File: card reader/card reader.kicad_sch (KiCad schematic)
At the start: 0 parts

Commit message: pdf
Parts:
- added A1: Arduino_Nano_v3.x, Module:Arduino_Nano, symbol MCU_Module:Arduino_Nano_v3.x
- added Q7: 2N7000, Package_TO_SOT_THT:TO-92_Inline, symbol Transistor_FET:2N7000
- added R1, R2, R26, R27, R3: 10k, symbol Device:R
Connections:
- new net: R2.2, R3.1
- new net +3.3V: Q7.2 (G), R26.1
- new net +5V: R27.1
- new net GND: R3.2
- new net RX_ARDUINO: Q7.3 (D), R27.2
- new net RX_RFID: R1.2, R2.1
- new net TX_ARDUINO: R1.1
- new net TX_RFID: Q7.1 (S), R26.2
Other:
- note added: "Adaptamos la tensión de 5 V a ~3.3 V (Arduino -> RFID reader)"
- note added: "Definir si se usa SPI o serial por soft. Seguramente si es spi se necesitan 3/4 conversores, si es serial solo 1 activo 1 pasivo. si es I2C idem serial"
- note added: "Esto es SPI seguro, al parecer es hard-wired"
- note added: "Subimos la tensión de 3.3 V a 5 V (RFID reader -> Arduino)"
- note added: "https://circuitdigest.com/microcontroller-projects/interfacing-rfid-reader-module-with-arduino"

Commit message: lolin module
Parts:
- removed A1: Arduino_Nano_v3.x, Module:Arduino_Nano, symbol MCU_Module:Arduino_Nano_v3.x
- removed Q7: 2N7000, Package_TO_SOT_THT:TO-92_Inline, symbol Transistor_FET:2N7000
- removed R1, R2, R26, R27, R3: 10k, symbol Device:R
- added M1: RFID-RC522, RFID-RC522:RFID-RC522, symbol RFID-RC522:RFID-RC522
- added U1: NodeMCU1.0(ESP-12E), ESP8266:NodeMCU-LoLinV3, symbol ESP8266:NodeMCU1.0(ESP-12E)
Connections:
- net +3.3V: now also M1.8 (3V3), U1.16 (3.3V)
- net GND: now also M1.6 (GND), U1.17 (GND)
- new net miso: M1.4 (MISO), U1.22 (D6(GPIO12))
- new net mosi: M1.3 (MOSI), U1.21 (D7(GPIO13))
- new net rst: M1.7 (RST), U1.27 (D3(GPIO0))
- new net sck: M1.2 (SCK), U1.23 (D5(GPIO14))
- new net sda: M1.1 (SDA), U1.26 (D4(GPIO2))
- no-connect marks 0 -> 1
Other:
- note added: "RFID RC522 (SPI) -> NodeMCU v1 (ESP-12E) SDA (SS) -> D4 (GPIO2) SCK -> D5 (GPIO14) MOSI -> D7 (GPIO13) MISO -> D6 (GPIO12) RST -> D3 (GPIO0) 3V3 -> 3V3 GND -> GND"
- note removed: "Adaptamos la tensión de 5 V a ~3.3 V (Arduino -> RFID reader)"
- note removed: "Definir si se usa SPI o serial por soft. Seguramente si es spi se necesitan 3/4 conversores, si es serial solo 1 activo 1 pasivo. si es I2C idem serial"
- note removed: "Esto es SPI seguro, al parecer es hard-wired"
- note removed: "Subimos la tensión de 3.3 V a 5 V (RFID reader -> Arduino)"
- note removed: "https://circuitdigest.com/microcontroller-projects/interfacing-rfid-reader-module-with-arduino"

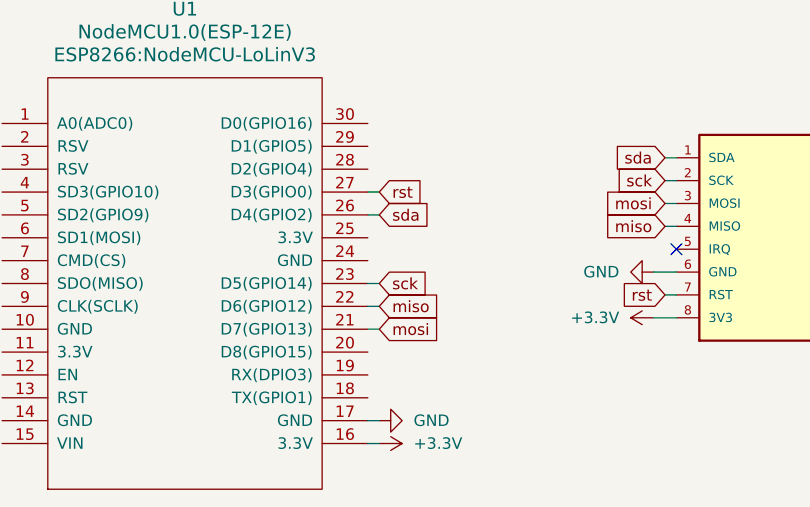
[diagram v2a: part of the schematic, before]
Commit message: ajustes,  1 nodemcu anda mal
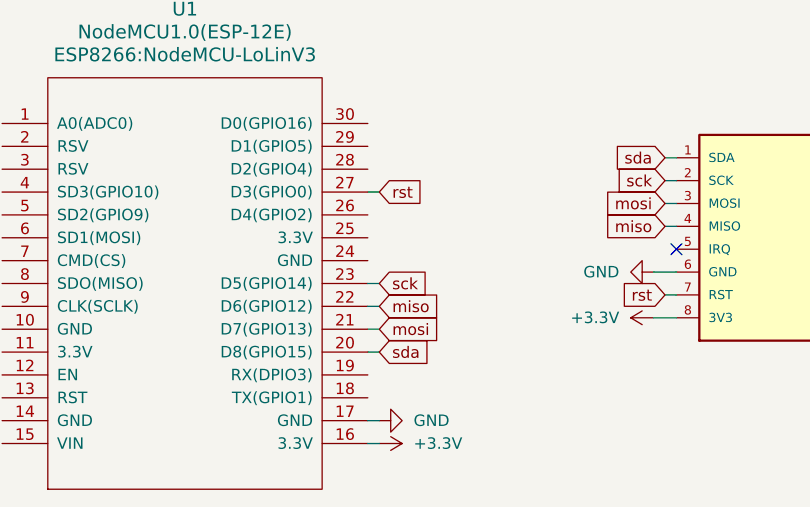
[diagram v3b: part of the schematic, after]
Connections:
- net sda: now also U1.20 (D8(GPIO15)); no longer U1.26 (D4(GPIO2))
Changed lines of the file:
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@@
 	(wire
 		(pts
-			(xy 125.73 102.87) (xy 124.46 102.87)
+			(xy 157.48 99.06) (xy 158.75 99.06)
 		)
 		(stroke
@@
 	(wire
 		(pts
-			(xy 157.48 99.06) (xy 158.75 99.06)
+			(xy 124.46 118.11) (xy 125.73 118.11)
 		)
 		(stroke
@@
 	(global_label "sda"
 		(shape input)
-		(at 125.73 102.87 0)
+		(at 125.73 118.11 0)
 		(fields_autoplaced yes)
 		(effects
@@
 		)
 		(property "Intersheetrefs" "${INTERSHEET_REFS}"
-			(at 132.0413 102.87 0)
+			(at 132.0413 118.11 0)
 			(effects
 				(font
